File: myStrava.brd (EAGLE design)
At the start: 64.8 x 45.4 mm, 27 parts, among them U1 ADXL345, U2 MAX1704X, U3 BMP180, U4 GTK

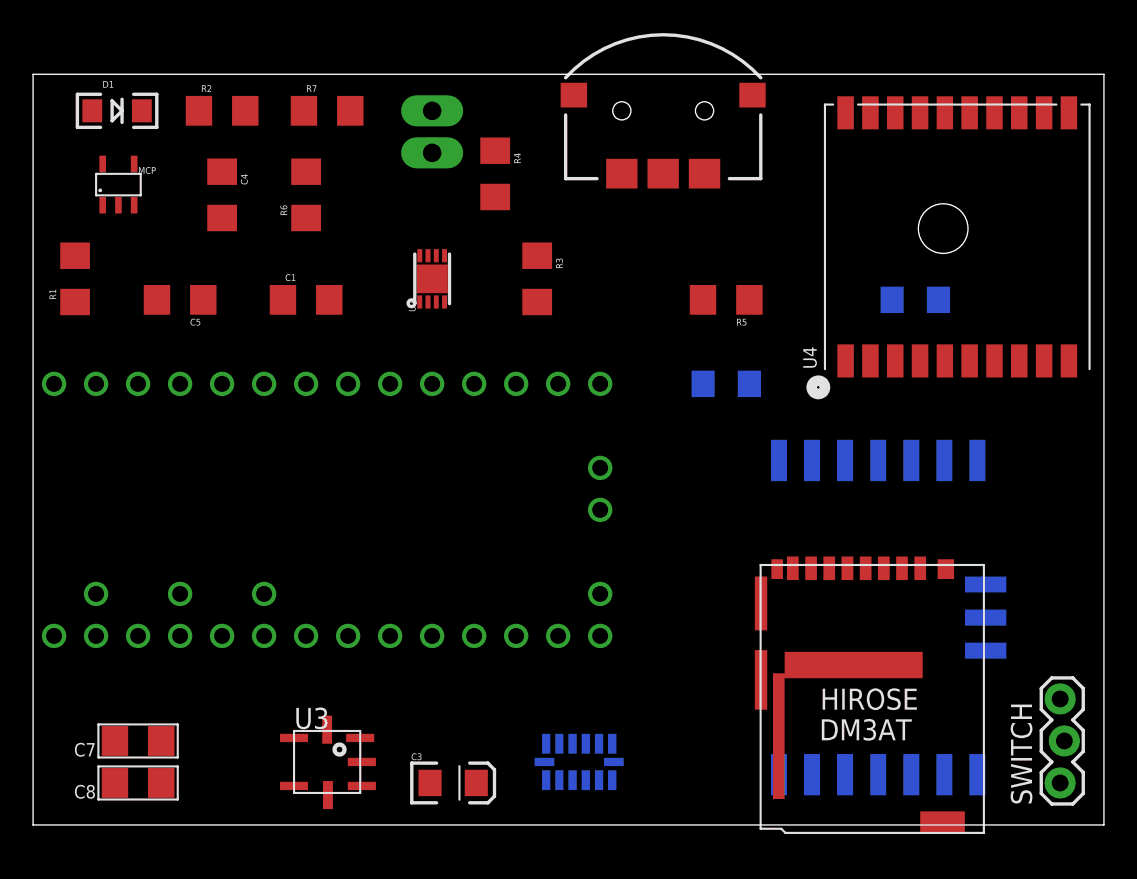
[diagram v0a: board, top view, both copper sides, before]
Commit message: Premiere board complete, manque l'ecran !
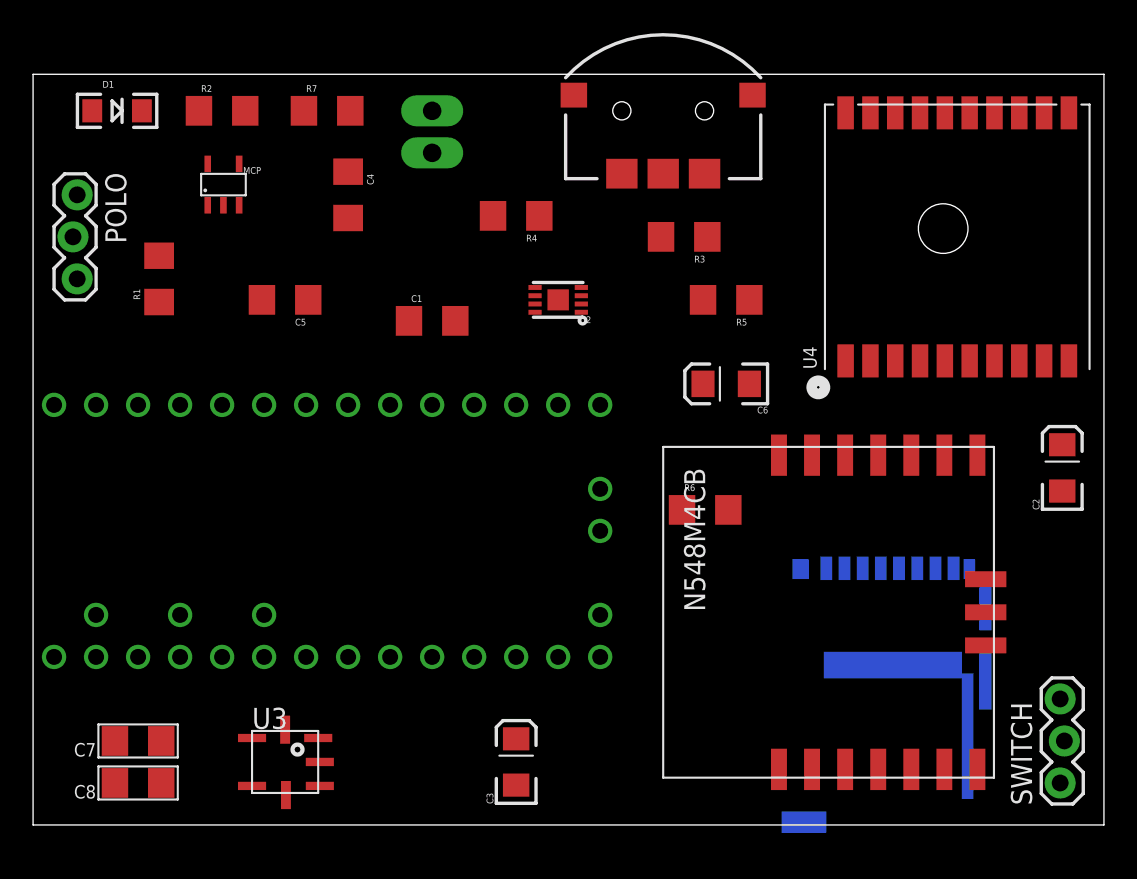
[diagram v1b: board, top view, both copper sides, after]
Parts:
- removed U1: ADXL345, SparkFun-Sensors:LGA14
- added POLO: (no value), SparkFun-Connectors:1X03_LOCK
- moved R6 30.7 mm to (40.6, 19.1), turned to 0 degrees
- moved U$10 20.3 mm to (38.1, 22.9), flipped to the top, turned to 270 degrees
- moved C2 13.5 mm to (62.2, 21.6), flipped to the top, turned to 90 degrees
- moved R3 9.25 mm to (39.4, 35.6), turned to 180 degrees
- moved U2 7.73 mm to (31.8, 31.8), turned to 180 degrees
- moved C1 7.73 mm to (24.1, 30.5)
- moved C4 7.62 mm to (19.1, 38.1)
- moved C5 6.35 mm to (15.2, 31.8)
- moved MCP 6.35 mm to (10.2, 38.1)
- moved R1 5.08 mm to (7.62, 33.0)
- moved C3 4.02 mm to (29.2, 3.81), turned to 90 degrees
- moved R4 2.84 mm to (29.2, 36.8), turned to 180 degrees
- moved U3 2.54 mm to (15.2, 3.81)
- moved U$2 1.27 mm to (19.1, 17.8)
- flipped C6 to the top
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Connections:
- removed net N$3: U$1.CLK, U$2.13, U1.14
- new net N$25: U$1.MOSI, U$2.12
- net GND: no longer U$2.AGND, U1.2, U1.4, U1.5
- net GND-ISO: now also POLO.2, U$2.AGND
- net N$1: no longer U1.12
- net N$19: now also SWITCH.2; no longer R3.1, R4.1, SWITCH.3
- net N$2: now also POLO.1, R3.1, R4.1, SWITCH.3; no longer U$1.MOSI, U$2.12, U1.13
- net N$6: now also U$1.CLK, U$2.13; no longer U$2.15/A1, U1.7
- net V+: now also POLO.3; no longer SWITCH.2
- net VCC: no longer U1.1, U1.6

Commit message: Bare metal !!!
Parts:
- removed MCP: MCP73831, BaseApp:5PIN_SOT23
- removed POLO: (no value), SparkFun-Connectors:1X03_LOCK
- removed U$1: DM3AT, HIROSE-DM3AT:DM3AT
- removed U$10: ANTAP28, ANTAP28:ANTAP
- removed U$2: TEENSY_3.1+4, Teensy_3_Series_Board_v1.0:TEENSY_3.1+4
- removed U$25: NAV_SWITCHSMD, SparkFun-Electromechanical:NAV_SWITCH
- removed U2: MAX1704X, SparkFun-PowerIC:TDFN-8
- removed U3: BMP180, SparkFun-Sensors:BMP180
- removed U4: GTK, adafruit:FGPMMOPA6H
- added BMP180: BMP180, SparkFun-Sensors:BMP180
- added C10, C11, C9: 0.1uF, microbuilder:1206
- added JTAG: 2X5_0.05"_CORTEX_DEBUGTH_NOKEY_UNSHROUDED, con-cortex:2X5_0.05"_TH_NS
- added LDO33: 3.3V/150mA, SparkFun-PowerIC:SOT23-5
- added MAX17043: MAX1704X, SparkFun-PowerIC:TDFN-8
- added MCP73831: MCP73831, BaseApp:5PIN_SOT23
- added MK20DN512: MK20DN512, MK20DN512:LQFP-100
- added MT3339: GTK, adafruit:FGPMMOPA6H
- added N550: ANTAP28, ANTAP28:ANTAP
- added NAV: NAV_SWITCHSMD, SparkFun-Electromechanical:NAV_SWITCH
- added R10, R11, R12, R13, R14: 10k, SparkFun-Resistors:1206
- added R8, R9: 33ohm, SparkFun-Resistors:1206
- added SD: DM3AT, HIROSE-DM3AT:DM3AT
- added SHARP: SHARP27, sharp:SHARP27
- added SST25: FLASH, FlashMem:SOIC8
- added USB: USB-MICROB, SparkFun-Connectors:USB-MICROB
- added Y1: 16MHz, SparkFun-FreqCtrl:HC49U-V
- C2, C3, C6: device SparkFun-Capacitors:EIA3216 -> microbuilder:1206
- SWITCH: value (none) -> NAVI
- moved SWITCH 70.0 mm to (3.07, 40.0), turned to 270 degrees
- moved R6 37.3 mm to (7.73, 36.7), flipped to the bottom, turned to 90 degrees
- moved C8 33.5 mm to (39.8, 4.78), flipped to the bottom, turned to 270 degrees
- moved C2 26.1 mm to (38.0, 31.3), turned to 270 degrees
- moved C3 22.2 mm to (7.98, 10.2)
- moved C4 19.1 mm to (2.24, 29.1)
- moved D1 19.0 mm to (24.1, 42.8), turned to 180 degrees
- moved R4 18.2 mm to (12.6, 29.4), turned to 90 degrees
- moved C7 17.9 mm to (23.8, 9.34), turned to 0 degrees
- moved C5 16.9 mm to (31.6, 36.2), flipped to the bottom, turned to 270 degrees
- moved BATT 16.5 mm to (7.71, 42.5), turned to 0 degrees
- moved R5 15.1 mm to (31.6, 42.8), flipped to the bottom, turned to 0 degrees
- moved R1 6.65 mm to (2.24, 29.1), flipped to the bottom
- moved C6 5.26 mm to (47.0, 25.2), flipped to the bottom, turned to 0 degrees
- moved R2 4.85 mm to (16.3, 42.8), turned to 180 degrees
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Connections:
- removed net AREF: U$2.AREF
- removed net GND-ISO: BATT.2, C1.1, C4.2, C5.2, MCP.P$2, POLO.2, R1.1, R7.2, U$2.AGND, U2.1, U2.4, U2.EP
- removed net N$10: U$2.8, U4.P$10
- removed net N$11: U$10.SUSPEND, U$2.17/A3
- removed net N$12: U$10.SLEEP, U$2.21/A7
- removed net N$13: U$10.RST, U$2.23/A9
- removed net N$15: U$10.RX, U$2.10
- removed net N$24: U$2.22/A8, U$25.1
- removed net N$5: U$1.CS, U$2.2
- removed net N$6: U$1.CLK, U$2.13
- removed net N$9: U$2.7, U4.P$9
- removed net SCL: R5.2, U$2.19/A5, U2.7, U3.5
- removed net SDA: R6.2, U$2.18/A4, U2.8, U3.6
- removed net V+: POLO.3, U$2.VIN
- removed net VCC: C2.A, C3.A, C6.A, C7.1, C8.1, R5.1, R6.1, U$1.VCC, U$10.VCC, U$2.3.3V, U$2.3.3V1, U3.2, U3.3, U4.P$1
- new net MK_DI: MK20DN512.79, SD.MISO, SST25.SO
- new net MK_DO: MK20DN512.78, SD.MOSI, SHARP.MOSI, SST25.SI
- new net MK_RX1: MK20DN512.62, MT3339.P$9
- new net MK_RX3: MK20DN512.95, N550.TX
- new net MK_SCL: BMP180.SCL_, MAX17043.7, MK20DN512.55, R5.2
- new net MK_SCLK: MK20DN512.77, SD.CLK, SHARP.SCK, SST25.SCK
- new net MK_SDA: BMP180.SDA_, MAX17043.8, MK20DN512.56, R6.2
- new net MK_TX1: MK20DN512.63, MT3339.P$10
- new net MK_TX3: MK20DN512.96, N550.RX
- new net N$26: R11.1, SHARP.EXTCOMM
- new net N$27: C11.1, R12.1, SHARP.DISP
- new net N$29: MK20DN512.64, NAV.2
- new net N$30: MK20DN512.65, NAV.T
- new net N$31: MK20DN512.53, NAV.1
- new net N$32: MK20DN512.70, SST25.CE
- new net N$33: R14.1, SST25.WP
- new net N$34: R13.2, SST25.HOLD
- new net N$35: JTAG.10, MK20DN512.52
- new net TCLK: JTAG.4, MK20DN512.34
- new net TDI: JTAG.8, MK20DN512.35
- new net TDO: JTAG.6, MK20DN512.36
- new net TMS: JTAG.2, MK20DN512.37
- new net USB1_DM_N: R9.1, USB.D-
- new net USB1_DP_P: R8.1, USB.D+
- new net USB_DM_N: MK20DN512.11, R9.2
- new net USB_DP_P: MK20DN512.10, R8.2
- new net VCC-ISO: LDO33.1, LDO33.3, R3.1, R4.1, SWITCH.3
- new net VDD: BMP180.VDD, BMP180.VDDIO, C2.1, C3.1, C6.1, C7.1, C8.1, C9.1, JTAG.1, LDO33.5, MK20DN512.12, MK20DN512.22, MK20DN512.23, MK20DN512.30, MK20DN512.40, MK20DN512.48, MK20DN512.61, MK20DN512.75, MK20DN512.8, MK20DN512.89, MT3339.P$1, N550.VCC, R12.2, R13.1, R14.2, R5.1, R6.1, SD.VCC, SHARP.VDD, SHARP.VDDA, SST25.VDD
- net GND: now also BATT.2, BMP180.GND_, C1.1, C10.2, C11.2, C2.2, C3.2, C4.2, C5.2, C6.2, C9.2, JTAG.3, JTAG.5, JTAG.9, LDO33.2, MAX17043.1, MAX17043.4, MAX17043.EP, MCP73831.P$2, MK20DN512.24, MK20DN512.25, MK20DN512.41, MK20DN512.49, MK20DN512.60, MK20DN512.74, MK20DN512.88, MK20DN512.9, MT3339.P$12, MT3339.P$19, MT3339.P$3, MT3339.P$8, N550.GND, N550.GND2, NAV.C, R1.1, R10.1, R11.2, R7.2, SD.GND, SHARP.VSS, SHARP.VSSA, SST25.VSS, USB.GND, USB.MT1, USB.MT2; no longer C2.C, C3.C, C6.C, U$1.GND, U$10.BR1, U$10.GND, U$10.GND2, U$10.P$12, U$10.PORTSEL, U$10.SCLK, U$10.SPD_SEL, U$2.GND, U$2.GND1, U$25.C, U3.7, U4.P$12, U4.P$19, U4.P$3, U4.P$8
- net N$1: now also MK20DN512.71, SD.CS; no longer U$1.MISO, U$2.11
- net N$14: now also MK20DN512.51, Y1.2; no longer U$10.BOOT, U$2.5
- net N$16: now also MCP73831.P$5; no longer MCP.P$5
- net N$17: now also MCP73831.P$1; no longer MCP.P$1
- net N$18: now also MCP73831.P$4, USB.VBUS; no longer MCP.P$4, U$2.VUSB
- net N$19: now also MK20DN512.50, Y1.1; no longer BATT.1, C5.1, MCP.P$3, SWITCH.2
- net N$2: now also BATT.1, C5.1, MCP73831.P$3, SWITCH.2; no longer POLO.1, R3.1, R4.1, SWITCH.3
- net N$21: now also MK20DN512.97, N550.BR1; no longer U$10.TX, U$2.9
- net N$22: now also MK20DN512.72, SHARP.CS; no longer U$2.14/A0, U$25.2
- net N$23: now also C10.1, MK20DN512.26; no longer U$2.16/A2, U$25.T
- net N$25: now also R10.2, SHARP.EXTMODE; no longer U$1.MOSI, U$2.12
- net N$4: now also MAX17043.2; no longer U2.2
- net N$7: now also MAX17043.3; no longer U2.3
- net N$8: now also MAX17043.6; no longer U2.6

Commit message: Routage initial
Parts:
- added SPK: FARNELL_SPK, Strutz Electronic Industries:IND-2020
- moved C5 23.0 mm to (8.79, 39.1), flipped to the top, turned to 0 degrees
- moved C10 21.5 mm to (18.7, 17.7), flipped to the bottom, turned to 90 degrees
- moved C3 20.2 mm to (27.2, 16.4), flipped to the bottom, turned to 180 degrees
- moved R3 18.5 mm to (20.4, 25.1), turned to 180 degrees
- moved R10 16.5 mm to (30.0, 14.0), flipped to the bottom, turned to 180 degrees
- moved SST25 13.1 mm to (42.2, 29.0), turned to 0 degrees
- moved C7 12.0 mm to (12.0, 12.0), flipped to the bottom, turned to 90 degrees
- moved R6 10.9 mm to (12.8, 27.0), turned to 180 degrees
- moved R4 10.1 mm to (20.9, 35.1)
- moved R12 9.55 mm to (5.51, 11.0), flipped to the bottom, turned to 270 degrees
- moved R14 9.02 mm to (61.7, 35.8), turned to 90 degrees
- moved C6 8.72 mm to (55.0, 21.9), flipped to the top, turned to 180 degrees
- moved MCP73831 7.80 mm to (10.4, 36.4), flipped to the top
- moved C8 6.62 mm to (40.2, 11.4)
- moved JTAG 6.15 mm to (7.50, 2.81), turned to 0 degrees
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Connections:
- net USB1_DP_P renamed USB1_DM_P
- net USB_DP_P renamed USB_DM_P
- new net N$3: MK20DN512.54, SPK.P$1
- net GND: now also SPK.P$2
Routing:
- net GND: track 0.00 -> 379.7 mm, vias 0 -> 7
- net VDD: track 0.00 -> 231.3 mm, vias 0 -> 7
- net N$21: track 0.00 -> 78.8 mm, vias 0 -> 1
- net MK_SCL: track 0.00 -> 70.1 mm, vias 0 -> 1
- net MK_SDA: track 0.00 -> 56.0 mm, vias 0 -> 2
- net N$27: track 0.00 -> 55.0 mm, vias 0 -> 1
- net N$18: track 0.00 -> 53.9 mm, vias 0 -> 2
- net MK_DO: track 0.00 -> 52.9 mm, vias 0 -> 4
- net MK_RX3: track 0.00 -> 51.5 mm, vias 0 -> 3
- net MK_TX3: track 0.00 -> 51.4 mm, vias 0 -> 3
- net MK_SCLK: track 0.00 -> 49.4 mm, vias 0 -> 4
- net N$22: track 0.00 -> 46.2 mm
- net N$35: track 0.00 -> 39.8 mm, vias 0 -> 1
- net N$34: track 0.00 -> 35.6 mm
- net N$3: track 0.00 -> 33.5 mm, vias 0 -> 2
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
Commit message: Envoi seeedstudio
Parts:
- moved C11 20.8 mm to (22.8, 29.4), turned to 180 degrees
- moved C3 20.6 mm to (46.1, 24.6), flipped to the top
- moved R7 15.1 mm to (30.5, 37.3), flipped to the top, turned to 270 degrees
- moved C1 11.5 mm to (17.4, 38.8), turned to 90 degrees
- moved C7 9.52 mm to (21.4, 10.2), turned to 0 degrees
- moved R3 9.01 mm to (21.1, 34.1), turned to 270 degrees
- moved R1 6.70 mm to (8.64, 31.1), flipped to the top, turned to 0 degrees
- moved R4 5.24 mm to (26.0, 33.9)
- moved MAX17043 4.19 mm to (24.2, 39.0)
- moved R12 3.77 mm to (2.44, 8.78), flipped to the top, turned to 90 degrees
- moved C6 3.47 mm to (58.4, 22.6)
- moved C2 2.72 mm to (34.5, 37.2), turned to 270 degrees
- moved R5 2.00 mm to (32.9, 41.2), flipped to the top, turned to 180 degrees
- moved C8 1.84 mm to (41.0, 13.1)
- moved C4 1.73 mm to (3.44, 30.4)
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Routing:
- net GND: track 379.7 -> 341.7 mm
- net N$34: track 35.6 -> 9.63 mm
- net N$27: track 55.0 -> 78.9 mm
- net N$21: track 78.8 -> 56.3 mm
- net N$22: track 46.2 -> 26.5 mm, vias 0 -> 2
- net MK_SCL: track 70.1 -> 51.8 mm, vias 1 -> 2
- net N$4: track 30.0 -> 12.9 mm
- net N$8: track 16.2 -> 4.94 mm, vias 1 -> 0
- net MK_SCLK: track 49.4 -> 41.2 mm
- net TDI: track 21.2 -> 27.8 mm
- net MK_DO: track 52.9 -> 46.8 mm
- net N$16: track 9.37 -> 3.57 mm, vias 1 -> 0
- net MK_TX3: track 51.4 -> 45.9 mm
- net VDD: track 231.3 -> 236.5 mm, vias 7 -> 5
- net N$29: track 29.6 -> 34.3 mm
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
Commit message: Avant autoroutage
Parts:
- removed MAX17043: MAX1704X, SparkFun-PowerIC:TDFN-8
- removed R13, R14: 10k, SparkFun-Resistors:1206
- added JTAG1: 2X5_0.05"_CORTEX_DEBUGTH_NOKEY_UNSHROUDED, con-cortex:2X5_0.05"_TH_NS
- added U$1: STC3100, STC3100:STC3100
- C1: value 1uF -> 220nF
- C4, C5: value 4.7uF -> 10uF
- R3: value 1k -> 200k/0.1%
- R4: value 180 -> 0.02
- R7: value 4.7k -> 1kOhms
- R8, R9: device SparkFun-Resistors:1206 -> SparkFun-Resistors:0805
- moved SPK 52.1 mm to (60.3, 26.9), turned to 180 degrees
- moved R12 44.0 mm to (37.3, 35.6), turned to 270 degrees
- moved MT3339 40.6 mm to (12.9, 16.1), turned to 180 degrees
- moved C6 34.0 mm to (25.0, 29.1), turned to 90 degrees
- moved N550 21.6 mm to (63.6, 1.49), flipped to the top, turned to 90 degrees
- moved R6 19.5 mm to (23.9, 42.9), turned to 0 degrees
- moved SST25 17.4 mm to (31.3, 15.4), turned to 90 degrees
- moved LDO33 17.4 mm to (30.0, 29.2), turned to 90 degrees
- moved R4 16.2 mm to (10.7, 28.7)
- moved JTAG 14.7 mm to (22.2, 3.51)
- moved R3 14.1 mm to (8.05, 28.6), flipped to the top
- moved C10 13.7 mm to (28.7, 8.03), turned to 270 degrees
- moved C7 13.7 mm to (34.5, 13.9)
- moved R7 13.4 mm to (19.3, 29.8), turned to 180 degrees
- moved C11 10.9 mm to (31.7, 35.6), turned to 270 degrees
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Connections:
- removed net N$29: MK20DN512.64, NAV.2
- removed net N$30: MK20DN512.65, NAV.T
- removed net N$31: MK20DN512.53, NAV.1
- removed net N$33: R14.1, SST25.WP
- removed net N$34: R13.2, SST25.HOLD
- new net N$10: N550.NONE1, NAV.2
- new net N$11: N550.SUSPEND, NAV.T
- new net N$12: N550.SLEEP, NAV.1
- new net N$13: N550.NONE2, NAV.C
- new net N$15: MK20DN512.69, SST25.WP
- new net N$24: MK20DN512.68, SST25.HOLD
- new net N$5: C1.1, R7.1, U$1.VIN
- new net N$6: BATT.2, R4.2, U$1.CG
- new net N$9: N550.PORTSEL, SPK.P$2
- new net VCC: JTAG1.1
- net GND: now also C1.2, JTAG1.3, JTAG1.5, JTAG1.9, R3.2, R4.1, U$1.GND; no longer BATT.2, C1.1, MAX17043.1, MAX17043.4, MAX17043.EP, NAV.C, R7.2, SPK.P$2
- net MK_SCL: now also U$1.SCL; no longer MAX17043.7
- net MK_SDA: now also U$1.SDA; no longer MAX17043.8
- net N$3: now also JTAG1.2, N550.RST; no longer MK20DN512.54, SPK.P$1
- net N$4: now also R3.1, U$1.ROSC; no longer C1.2, MAX17043.2, R3.2
- net N$7: now also JTAG1.4, N550.P$12; no longer MAX17043.3, R4.2
- net N$8: now also N550.SCLK, SPK.P$1; no longer MAX17043.6, R7.1
- net VCC-ISO: now also R7.2, U$1.VCC; no longer R3.1, R4.1
- net VDD: no longer R13.1, R14.2
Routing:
- net GND: track 341.7 -> 0.00 mm, vias 7 -> 0
- net VDD: track 236.5 -> 0.00 mm, vias 5 -> 0
- net N$27: track 78.9 -> 0.00 mm, vias 1 -> 0
- net N$21: track 56.3 -> 0.00 mm, vias 1 -> 0
- net N$18: track 54.0 -> 0.00 mm, vias 3 -> 0
- net MK_SDA: track 52.1 -> 0.00 mm, vias 4 -> 0
- net MK_SCL: track 51.8 -> 0.00 mm, vias 2 -> 0
- net MK_RX3: track 48.2 -> 0.00 mm, vias 1 -> 0
- net MK_DO: track 46.8 -> 0.00 mm, vias 4 -> 0
- net MK_TX3: track 45.9 -> 0.00 mm, vias 3 -> 0
- net MK_SCLK: track 41.2 -> 0.00 mm, vias 4 -> 0
- net N$35: track 35.6 -> 0.00 mm, vias 1 -> 0
- net VCC-ISO: track 34.4 -> 0.00 mm, vias 2 -> 0
- net N$29: track 34.3 -> 0.00 mm, vias 2 -> 0
- net N$3: track 31.2 -> 0.00 mm, vias 2 -> 0
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
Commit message: Version avec MK64
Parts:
- removed LDO33: 3.3V/150mA, SparkFun-PowerIC:SOT23-5
- added D2: OSRAM, SparkFun-LED:LED-1206
- added D3: Diode, adafruit:SOD-123FL
- added LDO0: 3.3V/150mA, SparkFun-PowerIC:SOT23-5
- added PTE2, PTE3, RX2, SCL, SDA: (no value), Exposed_pad:IND-2020
- added R13: 50ohms, SparkFun-Resistors:1206
- added R14: 10K, SparkFun-Resistors:1206
- added TX2: TX2, Exposed_pad:IND-2020
- moved Y1 38.3 mm to (34.8, 33.0), turned to 270 degrees
- moved JTAG 28.4 mm to (9.79, 29.0), turned to 90 degrees
- moved JTAG1 26.8 mm to (59.8, 36.4), turned to 90 degrees
- moved C6 22.4 mm to (47.4, 28.9), turned to 180 degrees
- moved C10 20.5 mm to (16.6, 24.5), flipped to the top
- moved R3 16.2 mm to (15.5, 43.0), flipped to the bottom, turned to 0 degrees
- moved R10 11.8 mm to (33.4, 9.64), turned to 0 degrees
- moved C7 9.73 mm to (44.0, 11.7), turned to 270 degrees
- moved R4 9.16 mm to (10.2, 37.9), flipped to the bottom, turned to 270 degrees
- moved C11 7.36 mm to (35.9, 41.7)
- moved C2 6.82 mm to (35.0, 41.7)
- moved R5 6.42 mm to (27.9, 39.3)
- moved MT3339 6.26 mm to (15.6, 10.5)
- moved SST25 4.51 mm to (27.6, 12.7), turned to 0 degrees
- moved C9 2.15 mm to (38.8, 34.0), turned to 90 degrees
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- renumbered U$1 to STC3100
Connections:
- removed net VDD: BMP180.VDD, BMP180.VDDIO, C2.1, C3.1, C6.1, C7.1, C8.1, C9.1, JTAG.1, LDO33.5, MK20DN512.12, MK20DN512.22, MK20DN512.23, MK20DN512.30, MK20DN512.40, MK20DN512.48, MK20DN512.61, MK20DN512.75, MK20DN512.8, MK20DN512.89, MT3339.P$1, N550.VCC, R12.2, R5.1, R6.1, SD.VCC, SHARP.VDD, SHARP.VDDA, SST25.VDD
- new net END_CHARGE: MCP73831.P$1, MK20DN512.53, R2.2
- new net MK_RX2: MK20DN512.2, RX2.P$1
- new net MK_TX2: MK20DN512.1, TX2.P$1
- new net MK_USB_DETECT: MK20DN512.6, R14.1
- new net N$28: MK20DN512.3, PTE2.P$1
- new net N$30: MK20DN512.4, PTE3.P$1
- new net N$31: MK20DN512.54, R13.1
- new net USB_V+: C4.1, D1.A, D3.A, MCP73831.P$4, R14.2, USB.VBUS
- net GND: now also LDO0.2; no longer LDO33.2
- net MK_SCL: now also SCL.P$1
- net MK_SDA: now also SDA.P$1
- net N$17: now also D2.C, R13.2; no longer MCP73831.P$1, R2.2
- net N$18: now also MK20DN512.94, N550.BR1; no longer C4.1, D1.A, MCP73831.P$4, USB.VBUS
- net N$21: now also MK20DN512.93, N550.SPD_SEL; no longer MK20DN512.97, N550.BR1
- net VCC: now also BMP180.VDD, BMP180.VDDIO, C2.1, C3.1, C6.1, C7.1, C8.1, C9.1, D2.A, JTAG.1, LDO0.5, MK20DN512.12, MK20DN512.22, MK20DN512.23, MK20DN512.30, MK20DN512.40, MK20DN512.48, MK20DN512.61, MK20DN512.75, MK20DN512.8, MK20DN512.89, MT3339.P$1, N550.VCC, R12.2, R5.1, R6.1, SD.VCC, SHARP.VDD, SHARP.VDDA, SST25.VDD
- net VCC-ISO: now also D3.C, LDO0.1, LDO0.3; no longer LDO33.1, LDO33.3
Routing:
- net USB_DM_N: track 0.00 -> 8.16 mm
- net USB_DM_P: track 0.00 -> 7.87 mm, vias 0 -> 2
- net USB1_DM_N: track 0.00 -> 4.40 mm
- net USB1_DM_P: track 0.00 -> 4.33 mm

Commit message: Circuit imprime avec bugs
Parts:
- moved C6 23.4 mm to (25.1, 21.8), turned to 0 degrees
- moved JTAG1 3.97 mm to (60.5, 40.2)
- moved D2 1.10 mm to (36.2, 22.3)
- moved R13 0.95 mm to (39.2, 25.2)
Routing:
- net GND: track 0.00 -> 335.2 mm, vias 0 -> 12
- net VCC: track 0.00 -> 228.6 mm, vias 0 -> 3
- net USB_V+: track 0.00 -> 109.7 mm, vias 0 -> 3
- net N$21: track 0.00 -> 58.8 mm, vias 0 -> 1
- net N$3: track 0.00 -> 54.5 mm
- net MK_RX3: track 0.00 -> 50.5 mm, vias 0 -> 3
- net MK_TX3: track 0.00 -> 49.1 mm, vias 0 -> 1
- net MK_DO: track 0.00 -> 46.5 mm, vias 0 -> 1
- net N$18: track 0.00 -> 45.7 mm, vias 0 -> 1
- net N$12: track 0.00 -> 43.2 mm
- net N$13: track 0.00 -> 42.1 mm
- net END_CHARGE: track 0.00 -> 41.4 mm, vias 0 -> 1
- net MK_DI: track 0.00 -> 39.1 mm, vias 0 -> 2
- net MK_SCLK: track 0.00 -> 39.0 mm, vias 0 -> 2
- net N$10: track 0.00 -> 38.2 mm, vias 0 -> 2
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- added copper zone on layer 1, net GND

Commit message: Modif pour le module D52Q
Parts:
- added LDO1: 3.3V/150mA, SparkFun-PowerIC:SOT23-5
- N550: device ANTAP28:ANTAP -> D52Q:ANTAP
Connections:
- removed net N$13: N550.NONE2, NAV.C
- new net VPERM: LDO1.5, MT3339.P$4
- net GND: now also LDO1.2, NAV.C; no longer N550.GND2
- net MK_RX3: now also N550.P017; no longer N550.TX
- net MK_TX3: now also N550.P016; no longer N550.RX
- net N$10: now also N550.P007, NAV.T; no longer N550.NONE1, NAV.2
- net N$11: now also N550.P006, NAV.2; no longer N550.SUSPEND, NAV.T
- net N$12: now also JTAG1.4, N550.SWDCLCK; no longer N550.SLEEP, NAV.1
- net N$18: now also N550.P015; no longer N550.BR1
- net N$2: now also LDO1.1, LDO1.3
- net N$21: now also N550.P014; no longer N550.SPD_SEL
- net N$3: now also N550.SWDIO; no longer N550.RST
- net N$7: now also N550.P002, NAV.1; no longer JTAG1.4, N550.P$12
- net N$8: now also N550.P011; no longer N550.SCLK
- net N$9: now also N550.P008; no longer N550.PORTSEL
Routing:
- net N$13: track 42.1 -> 0.00 mm
- net N$7: track 27.3 -> 66.8 mm, vias 1 -> 0
- net VPERM: track 0.00 -> 37.6 mm
- net N$2: track 12.5 -> 41.8 mm
- net N$3: track 54.5 -> 33.2 mm, vias 0 -> 1
- net N$10: track 38.2 -> 43.4 mm, vias 2 -> 0
- net N$1: track 23.0 -> 27.8 mm
- net N$12: track 43.2 -> 47.7 mm
- net VCC: track 228.6 -> 225.4 mm
- net MK_RX3: track 50.5 -> 47.4 mm, vias 3 -> 1
- net GND: track 335.2 -> 338.3 mm
- net MK_DO: track 46.5 -> 48.7 mm
- net N$18: track 45.7 -> 47.5 mm, vias 1 -> 3
- net N$21: track 58.8 -> 57.6 mm
- net MK_TX3: track 49.1 -> 48.1 mm
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- removed copper zone on layer 1, net GND
